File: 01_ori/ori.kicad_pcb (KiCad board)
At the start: 2 copper layers, 250 x 76.5 mm, 131 parts, among them J1 TYPE-C-31-M12_13, J2 AVR-ISP-6_mod, K1 KEYSW, K10 KEYSW, K11 KEYSW, K12 KEYSW, K13 KEYSW, K14 KEYSW, K15 KEYSW, K16 KEYSW, K17 KEYSW, K18 KEYSW, K19 KEYSW, K2 KEYSW, K20 KEYSW, K21 KEYSW, K22 KEYSW, K23 KEYSW, K24 KEYSW, K25 KEYSW, K26 KEYSW, K27 KEYSW, K28 KEYSW, K29 KEYSW, K3 KEYSW, K30 KEYSW, K31 KEYSW, K32 KEYSW, K33 KEYSW, K34 KEYSW, K35 KEYSW, K36 KEYSW, K37 KEYSW, K38 KEYSW, K39 KEYSW, K4 KEYSW, K40 KEYSW, K41 KEYSW, K42 KEYSW, K43 KEYSW, K44 KEYSW, K45 KEYSW, K46 KEYSW, K47 KEYSW, K48 KEYSW, K49 KEYSW, K5 KEYSW, K50 KEYSW, K51 KEYSW, K52 KEYSW, K6 KEYSW, K7 KEYSW, K8 KEYSW, K9 KEYSW, SW1 SW_PUSH, SW2 Rotary_Encoder_Switch, U1 ATMEGA32U4, U3 USBLC6-2SC6, Y1 16MHz

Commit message: new ESD protection
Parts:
- removed C7: 4.7nF, Capacitor_SMD:C_0805_2012Metric_Pad1.15x1.40mm_HandSolder
- removed CESD1: .1uF, Capacitor_SMD:C_0805_2012Metric_Pad1.15x1.40mm_HandSolder
- removed R5: 1M, Resistor_SMD:R_0805_2012Metric_Pad1.15x1.40mm_HandSolder
- removed U3: USBLC6-2SC6, acheron_Components:SOT-23-6
- added U2: PRTR5V0U2X, locallib:SOT143B, B.Cu at (115.5, 52.8)
- moved R4 3.36 mm to (108.2, 59.9)
- moved F1 3.36 mm to (110.8, 59.9)
- moved LED1 3.36 mm to (105.5, 59.9)
- moved R2 0.49 mm to (114.5, 58.2)
- moved R3 0.09 mm to (116.5, 58.2)
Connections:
- J1 pad S: Net-(C7-Pad1) -> GND
- R2 pad 2: Net-(R2-Pad2) -> DBUS-
- R3 pad 2: Net-(R3-Pad2) -> DBUS+
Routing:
- net Net-(C7-Pad1): track 29.9 -> 0.00 mm
- net VBUS: track 27.2 -> 20.1 mm
- net DBUS-: track 6.14 -> 12.3 mm
- net DBUS+: track 7.22 -> 13.0 mm
- net GND: track 64.5 -> 59.7 mm, vias 13 -> 12
- net Net-(R3-Pad2): track 3.00 -> 0.00 mm
- net Net-(R2-Pad2): track 3.00 -> 0.00 mm
- net D+: track 46.8 -> 49.3 mm
- net D-: track 46.9 -> 49.3 mm
- net VCC: track 252.5 -> 250.3 mm

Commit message: update rev silkscreen
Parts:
- U2: footprint locallib:SOT143B -> Keebio-Parts:SOT-143B
- moved C2 0.55 mm to (103.5, 84.7)
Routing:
- net VCC: track 250.3 -> 257.0 mm, vias 8 -> 9
- net ISP_Reset: track 116.0 -> 119.6 mm, vias 2 -> 4
- net GND: track 59.7 -> 58.1 mm, vias 12 -> 8
- net Net-(D26-Pad2): track 14.9 -> 15.7 mm
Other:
- board text added: "ori rev 1.1"
- board text added: "ori rev. 1.1 2021.09.26"
- board text removed: "Ori Rev 1.1"
- board text removed: "Ori Rev. 1.1 2021.09.03"

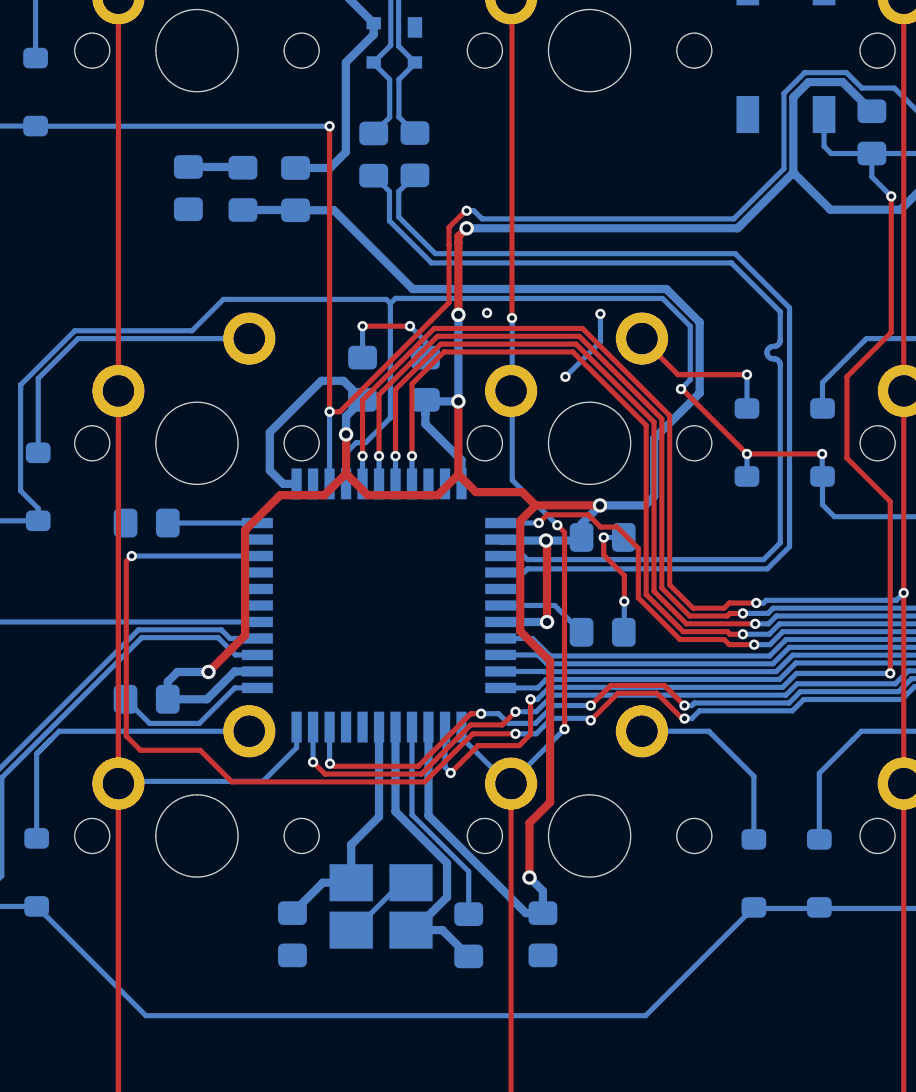
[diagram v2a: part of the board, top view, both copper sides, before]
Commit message: re-route VCC lines
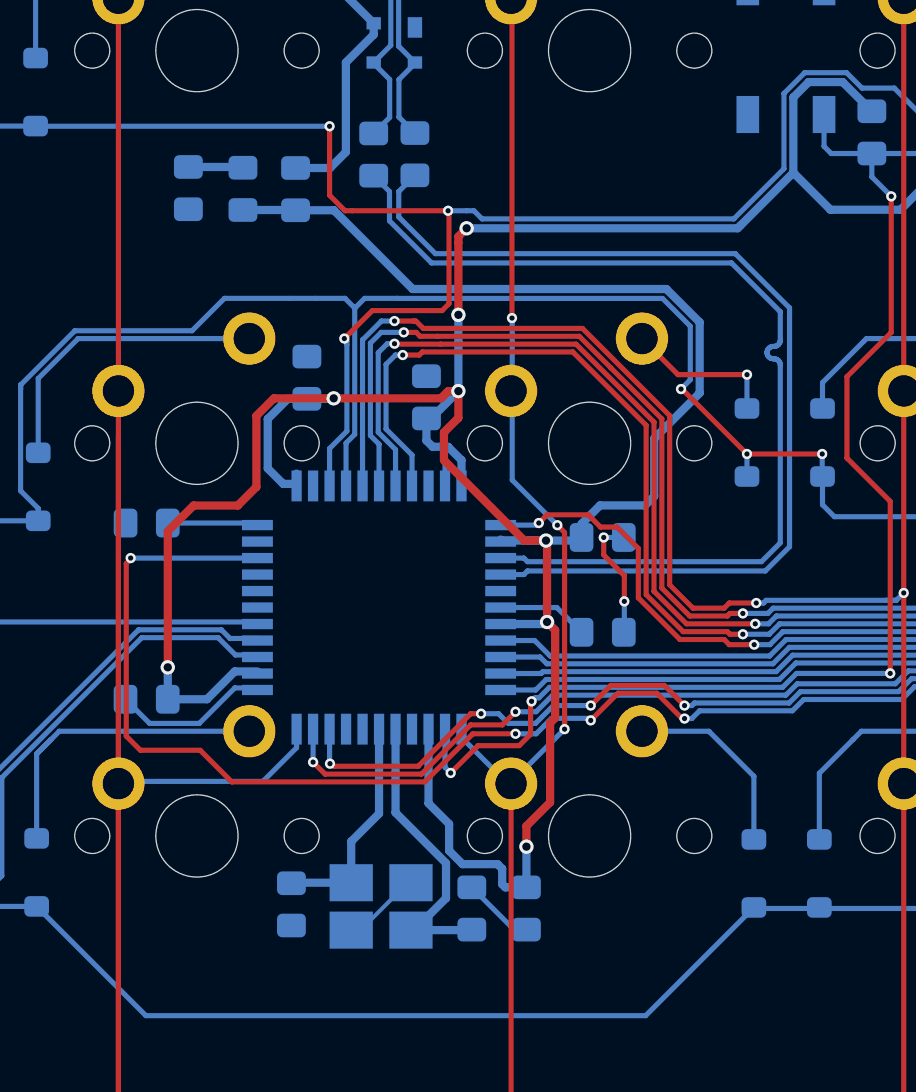
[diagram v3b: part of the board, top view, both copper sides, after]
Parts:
- moved C1 2.70 mm to (111.3, 69.0)
- moved C3 1.48 mm to (122.0, 94.8)
- moved CX2 1.45 mm to (110.5, 94.6)
- moved CX1 1.31 mm to (119.3, 94.8)
- moved C4 0.90 mm to (117.1, 70.0)
- moved U1 0.10 mm to (114.8, 80.2)
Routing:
- net GND: track 58.1 -> 43.3 mm, vias 8 -> 3
- net VCC: track 257.0 -> 245.7 mm, vias 9 -> 8
- net col6: track 154.7 -> 157.1 mm
- net col5: track 136.7 -> 138.9 mm
- net col4: track 118.5 -> 120.7 mm
- net row0: track 255.5 -> 253.3 mm
- net col3: track 100.1 -> 102.1 mm
- net row1: track 246.0 -> 245.0 mm
- net XTAL2: track 11.6 -> 10.9 mm
- net XTAL1: track 15.0 -> 14.5 mm

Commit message: add lucy text
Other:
- board text added: "lucy rev 1.1"
- board text added: "lucy rev. 1.1 2021.09.26"
- board text removed: "ori rev 1.1"
- board text removed: "ori rev. 1.1 2021.09.26"
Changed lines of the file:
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@@
   (gr_line (start 111.167865 42.179062) (end 119.813385 42.17901) (layer Edge.Cuts) (width 0.05))
   (gr_arc (start 119.813385 42.95625) (end 120.590625 42.95625) (angle -90) (layer Edge.Cuts) (width 0.05))
-  (gr_text "ori rev. 1.1 2021.09.26" (at 111.38288 116.5) (layer F.SilkS)
+  (gr_text "lucy rev. 1.1 2021.09.26" (at 111.38288 116.5) (layer F.SilkS)
     (effects (font (size 1.25 1.25) (thickness 0.2)))
   )
@@
     (effects (font (size 1.25 1.25) (thickness 0.2)) (justify mirror))
   )
-  (gr_text "ori rev 1.1" (at 115.48288 116.5) (layer B.SilkS)
+  (gr_text "lucy rev 1.1" (at 115.48288 116.5) (layer B.SilkS)
     (effects (font (size 1.25 1.25) (thickness 0.2)) (justify mirror))
   )
